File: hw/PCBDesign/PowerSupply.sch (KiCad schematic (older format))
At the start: 30 parts, among them J2 USB_B_Micro, J3 ExtBatt, U7 TP4056, U8 AMS1117-3.3

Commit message: HW updates. Testing out SPIFFS
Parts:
- J3: DigiKey (none) -> 455-1734-2-ND
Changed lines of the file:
@@
 F 2 "Connector_JST:JST_PH_B2B-PH-SM4-TB_1x02-1MP_P2.00mm_Vertical" H 6850 4850 50  0001 C CNN
 F 3 "~" H 6850 4850 50  0001 C CNN
+F 4 "455-1734-2-ND" H 6850 4850 50  0001 C CNN "DigiKey"
 	1    6850 4850
 	1    0    0    -1

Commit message: Investigate some USB issues. Add PCB remarks for revision 2
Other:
- note added: "BMB: 07/11/21\nConnect ID pin to ground. We want device mode only. Add test points."
- note added: "BMB: 07/11/21\nIncrease & balance the resistances on these leds. They are too bright."
- note added: "BMB: 07/11/21\nNeed a low dropout voltage regulator for battery power. This one is\nabsolutely horrendous. Consider a small SMPS."
- note added: "BMB: 07/11/21\nV_Batt_Sense needs to go through a voltage divider to translate to the\nADC range. Currently will blast +5V into the MCU."
- note added: "BMB: 07/11/21\nWhen no battery is connected, the charger IC won't enable thus\npreventing powering solely from USB. Need some kind of switch to\ndrive the regulator. Only need to handle 500mA."
- moved on the sheet: D8, D9, R60, R63
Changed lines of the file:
@@
 L Device:LED D9
 U 1 1 60590DC3
-P 8100 4900
-F 0 "D9" H 8093 5117 50  0000 C CNN
-F 1 "LED_3V3" H 8093 5026 50  0000 C CNN
-F 2 "LED_SMD:LED_0402_1005Metric" H 8100 4900 50  0001 C CNN
-F 3 "~" H 8100 4900 50  0001 C CNN
-F 4 "C72041" H 8100 4900 50  0001 C CNN "LCSC"
-	1    8100 4900
+P 5800 5750
+F 0 "D9" H 5793 5967 50  0000 C CNN
+F 1 "LED_3V3" H 5793 5876 50  0000 C CNN
+F 2 "LED_SMD:LED_0402_1005Metric" H 5800 5750 50  0001 C CNN
+F 3 "~" H 5800 5750 50  0001 C CNN
+F 4 "C72041" H 5800 5750 50  0001 C CNN "LCSC"
+	1    5800 5750
 	0    -1   -1   0
 $EndComp
@@
 L Device:LED D8
 U 1 1 605912DA
-P 7750 4900
-F 0 "D8" H 7743 5117 50  0000 C CNN
-F 1 "LED_5V0" H 7743 5026 50  0000 C CNN
-F 2 "LED_SMD:LED_0402_1005Metric" H 7750 4900 50  0001 C CNN
-F 3 "~" H 7750 4900 50  0001 C CNN
-F 4 "C72043" H 7750 4900 50  0001 C CNN "LCSC"
-	1    7750 4900
+P 5450 5750
+F 0 "D8" H 5443 5967 50  0000 C CNN
+F 1 "LED_5V0" H 5443 5876 50  0000 C CNN
+F 2 "LED_SMD:LED_0402_1005Metric" H 5450 5750 50  0001 C CNN
+F 3 "~" H 5450 5750 50  0001 C CNN
+F 4 "C72043" H 5450 5750 50  0001 C CNN "LCSC"
+	1    5450 5750
 	0    -1   -1   0
 $EndComp
-Text HLabel 7750 4450 1    50   BiDi ~ 0
+Text HLabel 5450 5300 1    50   BiDi ~ 0
 USB_+5V
 $Comp
 L Device:R_US R60
 U 1 1 6059151B
-P 7750 4600
-F 0 "R60" V 7545 4600 50  0000 C CNN
-F 1 "1.5k" V 7636 4600 50  0000 C CNN
-F 2 "Resistor_SMD:R_0402_1005Metric" V 7790 4590 50  0001 C CNN
-F 3 "~" H 7750 4600 50  0001 C CNN
-F 4 "C25867" H 7750 4600 50  0001 C CNN "LCSC"
-	1    7750 4600
+P 5450 5450
+F 0 "R60" V 5245 5450 50  0000 C CNN
+F 1 "1.5k" V 5336 5450 50  0000 C CNN
+F 2 "Resistor_SMD:R_0402_1005Metric" V 5490 5440 50  0001 C CNN
+F 3 "~" H 5450 5450 50  0001 C CNN
+F 4 "C25867" H 5450 5450 50  0001 C CNN "LCSC"
+	1    5450 5450
 	1    0    0    1
 $EndComp
@@
 L Device:R_US R63
 U 1 1 605924E4
-P 8100 4600
-F 0 "R63" V 7895 4600 50  0000 C CNN
-F 1 "330" V 7986 4600 50  0000 C CNN
-F 2 "Resistor_SMD:R_0402_1005Metric" V 8140 4590 50  0001 C CNN
-F 3 "~" H 8100 4600 50  0001 C CNN
-F 4 "C25104" H 8100 4600 50  0001 C CNN "LCSC"
-	1    8100 4600
+P 5800 5450
+F 0 "R63" V 5595 5450 50  0000 C CNN
+F 1 "330" V 5686 5450 50  0000 C CNN
+F 2 "Resistor_SMD:R_0402_1005Metric" V 5840 5440 50  0001 C CNN
+F 3 "~" H 5800 5450 50  0001 C CNN
+F 4 "C25104" H 5800 5450 50  0001 C CNN "LCSC"
+	1    5800 5450
 	1    0    0    1
 $EndComp
-Text HLabel 8100 4450 1    50   BiDi ~ 0
+Text HLabel 5800 5300 1    50   BiDi ~ 0
 V_Digital
 $Comp
 L power:GND #PWR04
 U 1 1 60596CB2
-P 7750 5050
-F 0 "#PWR04" H 7750 4800 50  0001 C CNN
-F 1 "GND" H 7755 4877 50  0000 C CNN
-F 2 "" H 7750 5050 50  0001 C CNN
-F 3 "" H 7750 5050 50  0001 C CNN
-	1    7750 5050
+P 5450 5900
+F 0 "#PWR04" H 5450 5650 50  0001 C CNN
+F 1 "GND" H 5455 5727 50  0000 C CNN
+F 2 "" H 5450 5900 50  0001 C CNN
+F 3 "" H 5450 5900 50  0001 C CNN
+	1    5450 5900
 	1    0    0    -1
 $EndComp
@@
 L power:GND #PWR05
 U 1 1 60596EA9
-P 8100 5050
-F 0 "#PWR05" H 8100 4800 50  0001 C CNN
-F 1 "GND" H 8105 4877 50  0000 C CNN
-F 2 "" H 8100 5050 50  0001 C CNN
-F 3 "" H 8100 5050 50  0001 C CNN
-	1    8100 5050
+P 5800 5900
+F 0 "#PWR05" H 5800 5650 50  0001 C CNN
+F 1 "GND" H 5805 5727 50  0000 C CNN
+F 2 "" H 5800 5900 50  0001 C CNN
+F 3 "" H 5800 5900 50  0001 C CNN
+	1    5800 5900
 	1    0    0    -1
 $EndComp
@@
 	-1   0    0    1
 $EndComp
+Text Notes 5000 1650 0    50   ~ 0
+BMB: 07/11/21\nConnect ID pin to ground. We want device mode only. Add test points.
+Text Notes 4100 2650 0    50   ~ 0
+BMB: 07/11/21\nWhen no battery is connected, the charger IC won't enable thus\npreventing powering solely from USB. Need some kind of switch to\ndrive the regulator. Only need to handle 500mA.
+Text Notes 6600 4250 0    50   ~ 0
+BMB: 07/11/21\nV_Batt_Sense needs to go through a voltage divider to translate to the\nADC range. Currently will blast +5V into the MCU.
+Text Notes 7650 3000 0    50   ~ 0
+BMB: 07/11/21\nNeed a low dropout voltage regulator for battery power. This one is\nabsolutely horrendous. Consider a small SMPS.
+Text Notes 4250 6250 0    50   ~ 0
+BMB: 07/11/21\nIncrease & balance the resistances on these leds. They are too bright.
 $EndSCHEMATC

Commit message: Improve the networking stability of RF24
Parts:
- removed BT1: Battery, symbol Device:Battery
- removed C36: 1uF, Capacitor_SMD:C_0805_2012Metric, symbol Device:C
- removed C38: 4.7uF, Capacitor_SMD:C_0805_2012Metric, symbol Device:C
- removed C40: 100n, Capacitor_SMD:C_0402_1005Metric, symbol Device:C
- removed D1: LED_PGD, LED_SMD:LED_0402_1005Metric, symbol Device:LED
- removed D2: LED_CHG, LED_SMD:LED_0402_1005Metric, symbol Device:LED
- removed J3: ExtBatt, Connector_JST:JST_PH_B2B-PH-SM4-TB_1x02-1MP_P2.00mm_Vertical, symbol Connector_Generic:Conn_01x02
- removed R73, R82, R83, R84: 100k, Resistor_SMD:R_0402_1005Metric, symbol Device:R_US
- removed R79: 10k, Resistor_SMD:R_0402_1005Metric, symbol Device:R_US
- removed R80, R81: 1.5k, Resistor_SMD:R_0402_1005Metric, symbol Device:R_US
- removed TP23, TP24: TestPoint, TestPoint:TestPoint_Pad_2.5x2.5mm, symbol Connector:TestPoint
- removed U7: TP4056, PMIC:TP4056_SOP-8-PP, symbol tp4056:TP4056
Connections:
- net labels removed: CHG_Sense, CHG_nEN, PGD_Sense, V_Batt_Sense, vBatt
- wire segments 74 -> 40
- no-connect marks 2 -> 0
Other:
- note removed: "BMB: 07/11/21\nConnect ID pin to ground. We want device mode only. Add test points."
- note removed: "BMB: 07/11/21\nNeed a low dropout voltage regulator for battery power. This one is\nabsolutely horrendous. Consider a small SMPS."
- note removed: "BMB: 07/11/21\nV_Batt_Sense needs to go through a voltage divider to translate to the\nADC range. Currently will blast +5V into the MCU."
- note removed: "BMB: 07/11/21\nWhen no battery is connected, the charger IC won't enable thus\npreventing powering solely from USB. Need some kind of switch to\ndrive the regulator. Only need to handle 500mA."
- moved on the sheet: C37, D8, D9, J2, R60, R63, TP25, TP26

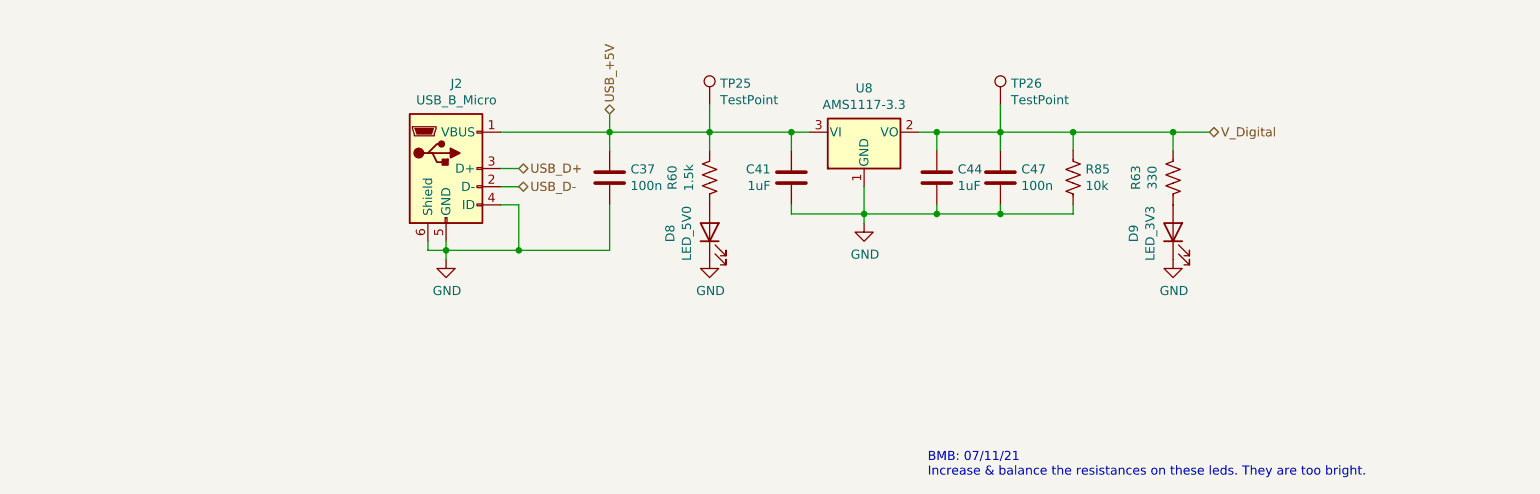
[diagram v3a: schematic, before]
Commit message: Start working on PCB rev 2.0
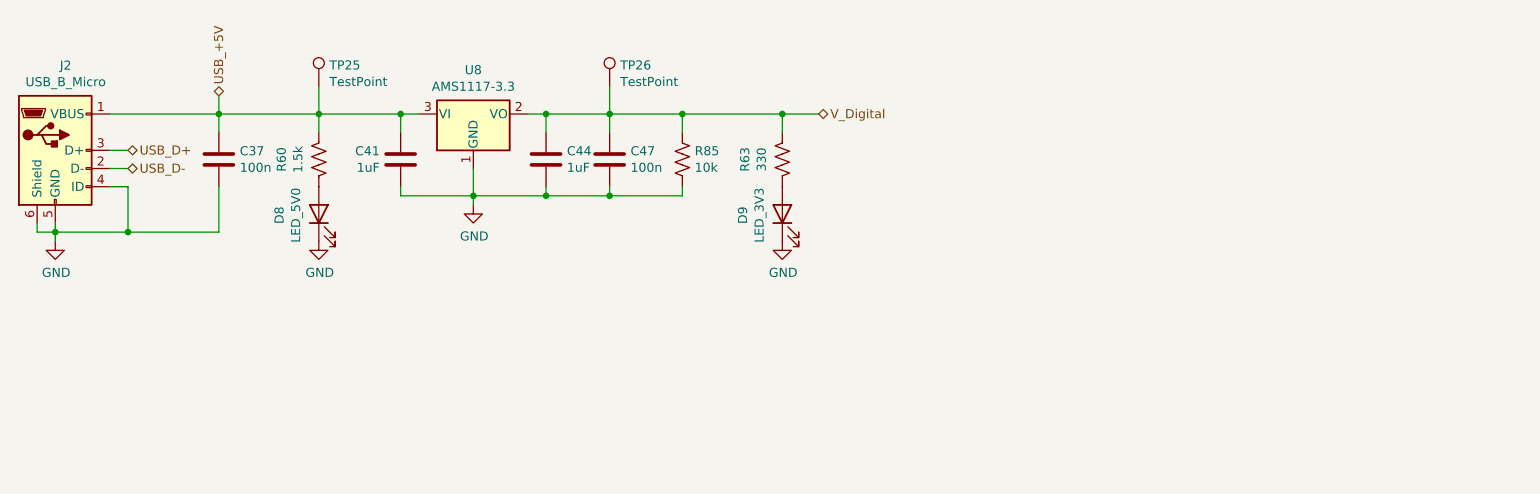
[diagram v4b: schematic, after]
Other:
- note removed: "BMB: 07/11/21\nIncrease & balance the resistances on these leds. They are too bright."
- moved on the sheet: C37, C41, C44, C47, D8, D9, J2, R60, R63, R85, TP25, TP26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

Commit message: Add more work on PCB v2 design
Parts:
- removed TP25, TP26: TestPoint, TestPoint:TestPoint_Pad_2.5x2.5mm, symbol Connector:TestPoint
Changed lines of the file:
@@
-	1    0    0    -1
-$EndComp
-$Comp
-L Connector:TestPoint TP?
-U 1 1 605EF9F2
-P 5250 3050
-AR Path="/6045890B/605EF9F2" Ref="TP?"  Part="1"
-AR Path="/604707FB/605EF9F2" Ref="TP?"  Part="1"
-AR Path="/60472222/605EF9F2" Ref="TP25"  Part="1"
-F 0 "TP25" H 5308 3168 50  0000 L CNN
-F 1 "TestPoint" H 5308 3077 50  0000 L CNN
-F 2 "TestPoint:TestPoint_Pad_2.5x2.5mm" H 5450 3050 50  0001 C CNN
-F 3 "~" H 5450 3050 50  0001 C CNN
-	1    5250 3050
-	1    0    0    -1
-$EndComp
-$Comp
-L Connector:TestPoint TP?
-U 1 1 605EFDA7
-P 6850 3050
-AR Path="/6045890B/605EFDA7" Ref="TP?"  Part="1"
-AR Path="/604707FB/605EFDA7" Ref="TP?"  Part="1"
-AR Path="/60472222/605EFDA7" Ref="TP26"  Part="1"
-F 0 "TP26" H 6908 3168 50  0000 L CNN
-F 1 "TestPoint" H 6908 3077 50  0000 L CNN
-F 2 "TestPoint:TestPoint_Pad_2.5x2.5mm" H 7050 3050 50  0001 C CNN
-F 3 "~" H 7050 3050 50  0001 C CNN
-	1    6850 3050
 	1    0    0    -1
 $EndComp
@@
 	4700 3100 4700 3200
 Wire Wire Line
-	5250 3050 5250 3200
-Wire Wire Line
-	6850 3050 6850 3200
-Wire Wire Line
 	7800 3200 7800 3300

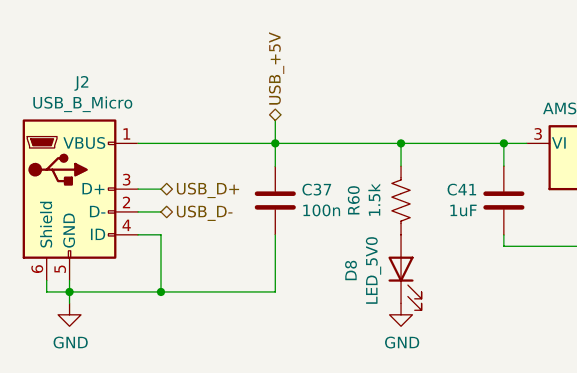
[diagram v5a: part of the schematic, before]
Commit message: Work further on v2.0 of controller pcb
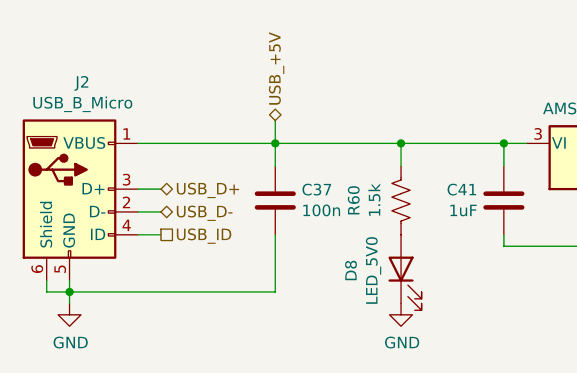
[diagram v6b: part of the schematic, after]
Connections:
- net GND: no longer J2.4 (ID)
- new net USB_ID: J2.4 (ID)
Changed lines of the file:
@@
 	4700 3600 4700 3850
-Wire Wire Line
-	4700 3850 4200 3850
 Wire Wire Line
 	4100 3200 4700 3200
@@
 	4100 3600 4200 3600
 Wire Wire Line
-	4200 3600 4200 3850
-Connection ~ 4200 3850
-Wire Wire Line
-	4200 3850 3800 3850
-Wire Wire Line
 	4700 3200 5250 3200
 Wire Wire Line
@@
 	8000 3200 7800 3200
 Connection ~ 7800 3200
+Wire Wire Line
+	3800 3850 4700 3850
+Text HLabel 4200 3600 2    50   UnSpc ~ 0
+USB_ID
 $EndSCHEMATC
